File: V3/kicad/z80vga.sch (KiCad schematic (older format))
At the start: 11 parts, among them J1000 Barrel_Jack_Switch, U1000 L7805

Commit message: still trying to make routes work
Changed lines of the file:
@@
 F0 "2000_Z80" 50
 F1 "2000_Z80.sch" 50
-F2 "A[0..19]" T R 5100 3800 50
-F3 "D[0..7]" T R 5100 4600 50
-F4 "WRITE" O R 5100 4000 50
-F5 "READ" O R 5100 3900 50
-F6 "ROM_CS" O R 5100 4300 50
-F7 "RAM_CS" O R 5100 4200 50
+F2 "D[0..7]" T R 5100 4600 50
+F3 "WRITE" O R 5100 4000 50
+F4 "READ" O R 5100 3900 50
+F5 "ROM_CS" O R 5100 4300 50
+F6 "RAM_CS" O R 5100 4200 50
+F7 "A[0..19]" O R 5100 3800 50
 $EndSheet
 Text Notes 7800 6950 0    118  ~ 24

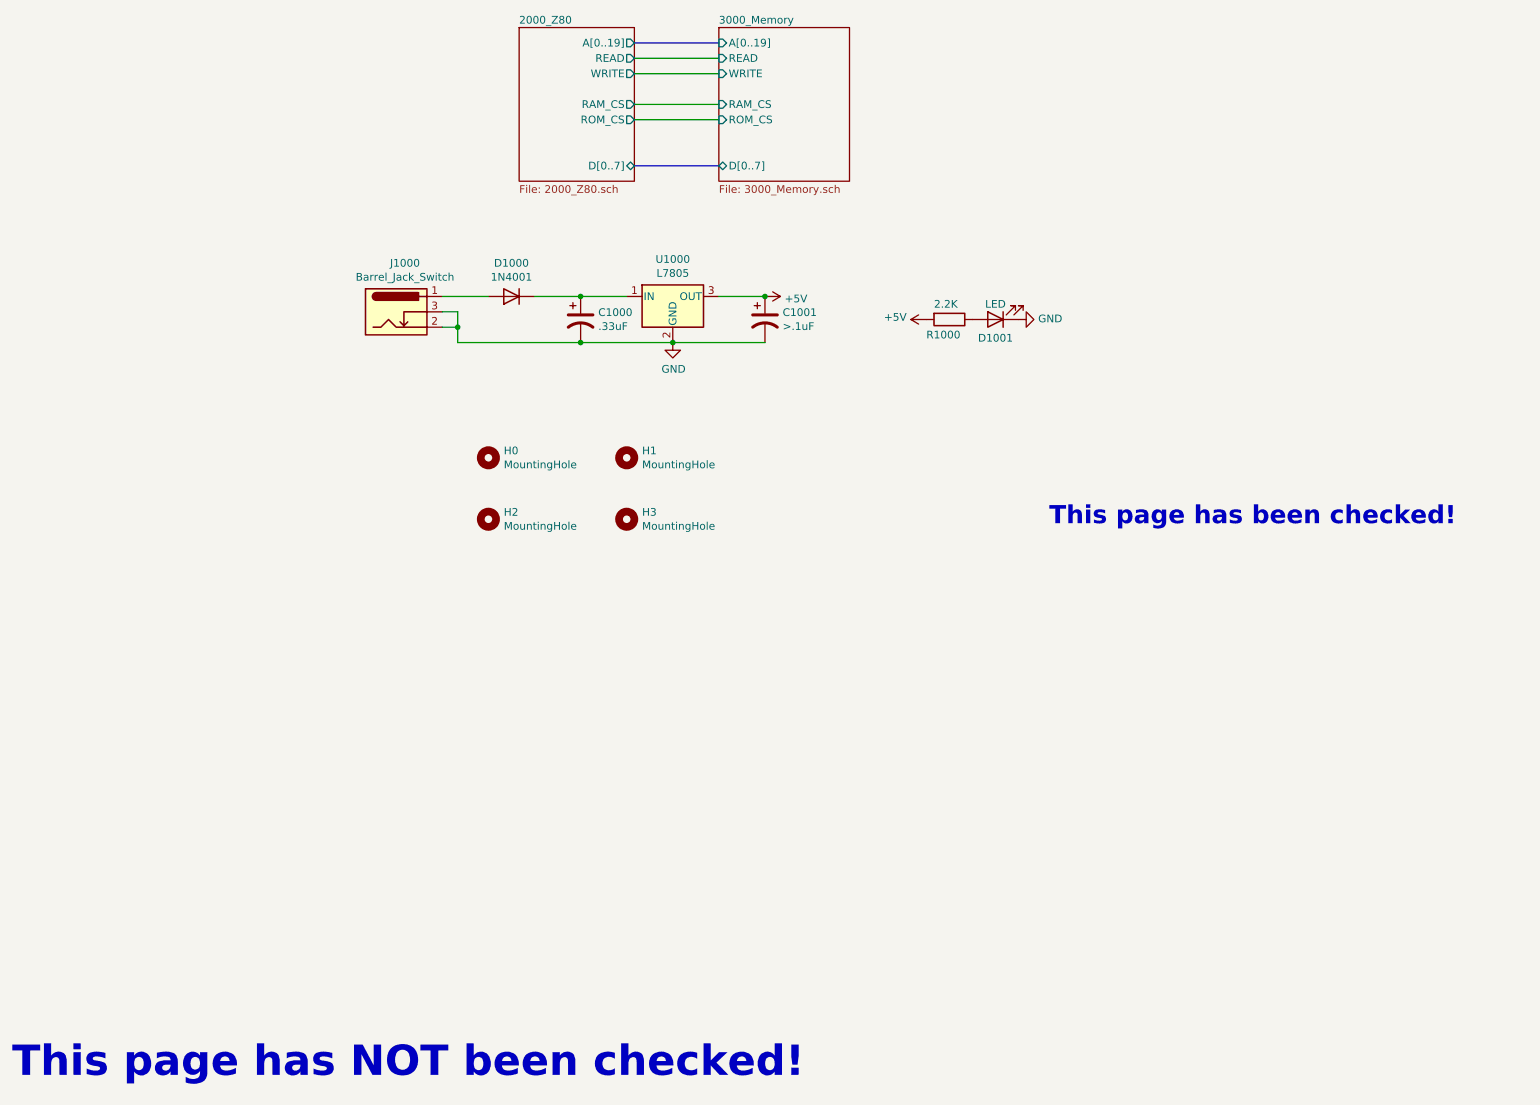
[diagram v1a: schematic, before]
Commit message: Completely redesigned board layout
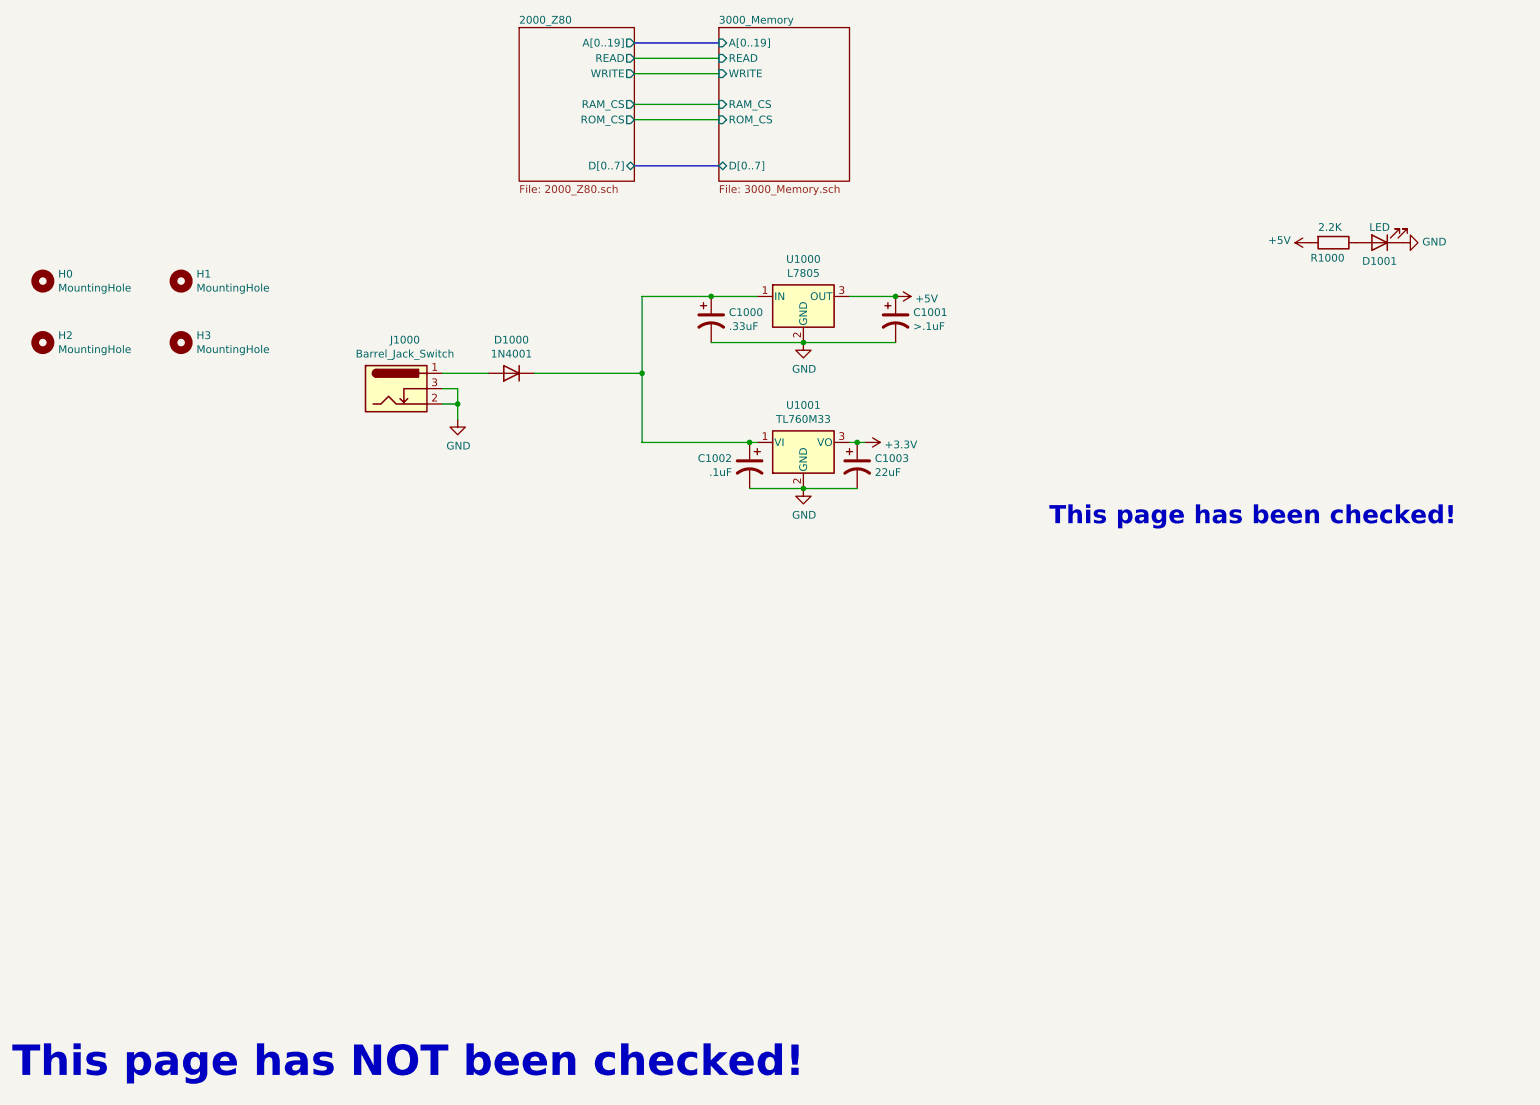
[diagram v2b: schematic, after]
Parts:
- added C1002: .1uF, Capacitor_THT:CP_Radial_D5.0mm_P2.00mm, symbol Device:CP1
- added C1003: 22uF, Capacitor_THT:CP_Radial_D5.0mm_P2.00mm, symbol Device:CP1
- added U1001: TL760M33, Package_TO_SOT_SMD:TO-252-3_TabPin2, symbol Regulator_Linear:LD39150DT33
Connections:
- net GND: now also C1002.2, C1003.2, U1001.2 (GND)
- net at C1000.1, D1000.1 (K), U1000.1 (IN): now also C1002.1, U1001.1 (VI)
- new net +3V3: C1003.1, U1001.3 (VO)
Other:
- moved on the sheet: C1000, C1001, D1000, D1001, H0, H1, H2, H3, J1000, R1000, U1000

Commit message: Final checks and DRC
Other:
- moved on the sheet: D1001, R1000
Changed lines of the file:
@@
 L Device:LED D?
 U 1 1 62A5A6D1
-P 9950 5100
+P 4150 7050
 AR Path="/6191B6A2/61EBDADB/62A5A6D1" Ref="D?"  Part="1"
 AR Path="/62A5A6D1" Ref="D1001"  Part="1"
-F 0 "D1001" H 9950 5250 50  0000 C TNN
-F 1 "LED" H 9950 5000 50  0000 C CNN
-F 2 "LED_THT:LED_D3.0mm" H 9950 5100 50  0001 C CNN
-F 3 "~" H 9950 5100 50  0001 C CNN
-	1    9950 5100
+F 0 "D1001" H 4150 7200 50  0000 C TNN
+F 1 "LED" H 4150 6950 50  0000 C CNN
+F 2 "LED_THT:LED_D3.0mm" H 4150 7050 50  0001 C CNN
+F 3 "~" H 4150 7050 50  0001 C CNN
+	1    4150 7050
 	-1   0    0    1
 $EndComp
@@
 L power:GND #PWR?
 U 1 1 62A5A6D8
-P 10100 5100
+P 4300 7050
 AR Path="/6191B6A2/61EBDADB/62A5A6D8" Ref="#PWR?"  Part="1"
 AR Path="/62A5A6D8" Ref="#PWR0123"  Part="1"
-F 0 "#PWR0123" H 10100 4850 50  0001 C CNN
-F 1 "GND" V 10105 4972 50  0000 R CNN
-F 2 "" H 10100 5100 50  0001 C CNN
-F 3 "" H 10100 5100 50  0001 C CNN
-	1    10100 5100
+F 0 "#PWR0123" H 4300 6800 50  0001 C CNN
+F 1 "GND" V 4305 6922 50  0000 R CNN
+F 2 "" H 4300 7050 50  0001 C CNN
+F 3 "" H 4300 7050 50  0001 C CNN
+	1    4300 7050
 	0    -1   -1   0
 $EndComp
@@
 L power:+5V #PWR0144
 U 1 1 62A5BC7A
-P 9500 5100
-F 0 "#PWR0144" H 9500 4950 50  0001 C CNN
-F 1 "+5V" V 9515 5228 50  0000 L CNN
-F 2 "" H 9500 5100 50  0001 C CNN
-F 3 "" H 9500 5100 50  0001 C CNN
-	1    9500 5100
+P 3700 7050
+F 0 "#PWR0144" H 3700 6900 50  0001 C CNN
+F 1 "+5V" V 3715 7178 50  0000 L CNN
+F 2 "" H 3700 7050 50  0001 C CNN
+F 3 "" H 3700 7050 50  0001 C CNN
+	1    3700 7050
 	0    -1   -1   0
 $EndComp
@@
 L Device:R R?
 U 1 1 62A654EB
-P 9650 5100
+P 3850 7050
 AR Path="/6191B6A2/61EBDADB/62542978/62A654EB" Ref="R?"  Part="1"
 AR Path="/62A654EB" Ref="R1000"  Part="1"
-F 0 "R1000" V 9750 4950 50  0000 L CNN
-F 1 "2.2K" V 9550 5000 50  0000 L CNN
-F 2 "Resistor_THT:R_Axial_DIN0309_L9.0mm_D3.2mm_P2.54mm_Vertical" V 9580 5100 50  0001 C CNN
-F 3 "~" H 9650 5100 50  0001 C CNN
-	1    9650 5100
+F 0 "R1000" V 3950 6900 50  0000 L CNN
+F 1 "2.2K" V 3750 6950 50  0000 L CNN
+F 2 "Resistor_THT:R_Axial_DIN0309_L9.0mm_D3.2mm_P2.54mm_Vertical" V 3780 7050 50  0001 C CNN
+F 3 "~" H 3850 7050 50  0001 C CNN
+	1    3850 7050
 	0    1    1    0
 $EndComp

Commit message: just totally redid the whole thing
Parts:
- removed C1000: .33uF, Capacitor_THT:CP_Radial_D5.0mm_P2.00mm, symbol Device:CP1
- removed C1001: >.1uF, Capacitor_THT:CP_Radial_D5.0mm_P2.00mm, symbol Device:CP1
- removed C1002: .1uF, Capacitor_THT:CP_Radial_D5.0mm_P2.00mm, symbol Device:CP1
- removed C1003: 22uF, Capacitor_THT:CP_Radial_D5.0mm_P2.00mm, symbol Device:CP1
- removed D1000: 1N4001, Diode_THT:D_DO-41_SOD81_P10.16mm_Horizontal, symbol Diode:1N4001
- removed J1000: Barrel_Jack_Switch, Connector_BarrelJack:BarrelJack_Horizontal, symbol Connector:Barrel_Jack_Switch
- removed U1000: L7805, Package_TO_SOT_SMD:TO-263-3_TabPin2, symbol Regulator_Linear:L7805
- removed U1001: TL760M33, Package_TO_SOT_SMD:TO-252-3_TabPin2, symbol Regulator_Linear:LD39150DT33
- R1000: footprint Resistor_THT:R_Axial_DIN0309_L9.0mm_D3.2mm_P2.54mm_Vertical -> Resistor_SMD:R_1206_3216Metric
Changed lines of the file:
@@
 $Descr A4 11693 8268
 encoding utf-8
-Sheet 1 9
+Sheet 1 8
 Title ""
 Date ""
@@
 Wire Wire Line
 	5100 4300 5650 4300
-$Comp
-L Regulator_Linear:L7805 U1000
-U 1 1 6255C02F
-P 6200 5450
-F 0 "U1000" H 6200 5692 50  0000 C CNN
-F 1 "L7805" H 6200 5601 50  0000 C CNN
-F 2 "Package_TO_SOT_SMD:TO-263-3_TabPin2" H 6225 5300 50  0001 L CIN
-F 3 "http://www.st.com/content/ccc/resource/technical/document/datasheet/41/4f/b3/b0/12/d4/47/88/CD00000444.pdf/files/CD00000444.pdf/jcr:content/translations/en.CD00000444.pdf" H 6200 5400 50  0001 C CNN
-	1    6200 5450
-	1    0    0    -1
-$EndComp
-$Comp
-L Device:CP1 C1000
-U 1 1 6255CCA4
-P 5600 5600
-F 0 "C1000" H 5715 5646 50  0000 L CNN
-F 1 ".33uF" H 5715 5555 50  0000 L CNN
-F 2 "Capacitor_THT:CP_Radial_D5.0mm_P2.00mm" H 5600 5600 50  0001 C CNN
-F 3 "~" H 5600 5600 50  0001 C CNN
-	1    5600 5600
-	1    0    0    -1
-$EndComp
-$Comp
-L Device:CP1 C1001
-U 1 1 6255DB35
-P 6800 5600
-F 0 "C1001" H 6915 5646 50  0000 L CNN
-F 1 ">.1uF" H 6915 5555 50  0000 L CNN
-F 2 "Capacitor_THT:CP_Radial_D5.0mm_P2.00mm" H 6800 5600 50  0001 C CNN
-F 3 "~" H 6800 5600 50  0001 C CNN
-	1    6800 5600
-	1    0    0    -1
-$EndComp
-Wire Wire Line
-	5600 5450 5900 5450
-Wire Wire Line
-	6500 5450 6800 5450
-Wire Wire Line
-	5600 5750 6200 5750
-Connection ~ 6200 5750
-Wire Wire Line
-	6200 5750 6800 5750
-$Comp
-L power:GND #PWR0119
-U 1 1 6255E2E4
-P 6200 5750
-F 0 "#PWR0119" H 6200 5500 50  0001 C CNN
-F 1 "GND" H 6205 5577 50  0000 C CNN
-F 2 "" H 6200 5750 50  0001 C CNN
-F 3 "" H 6200 5750 50  0001 C CNN
-	1    6200 5750
-	1    0    0    -1
-$EndComp
-$Comp
-L power:+5V #PWR0141
-U 1 1 6255EB09
-P 6800 5450
-F 0 "#PWR0141" H 6800 5300 50  0001 C CNN
-F 1 "+5V" V 6815 5578 50  0000 L CNN
-F 2 "" H 6800 5450 50  0001 C CNN
-F 3 "" H 6800 5450 50  0001 C CNN
-	1    6800 5450
-	0    1    1    0
-$EndComp
-Connection ~ 6800 5450
-$Comp
-L Connector:Barrel_Jack_Switch J1000
-U 1 1 62560114
-P 3550 6050
-F 0 "J1000" H 3607 6367 50  0000 C CNN
-F 1 "Barrel_Jack_Switch" H 3607 6276 50  0000 C CNN
-F 2 "Connector_BarrelJack:BarrelJack_Horizontal" H 3600 6010 50  0001 C CNN
-F 3 "~" H 3600 6010 50  0001 C CNN
-	1    3550 6050
-	1    0    0    -1
-$EndComp
-Wire Wire Line
-	3850 5950 4150 5950
-Wire Wire Line
-	3850 6050 3950 6050
-Wire Wire Line
-	3950 6050 3950 6150
-Wire Wire Line
-	3950 6150 3850 6150
-Wire Wire Line
-	3950 6150 3950 6250
-Connection ~ 3950 6150
-$Comp
-L Diode:1N4001 D1000
-U 1 1 62563A78
-P 4300 5950
-F 0 "D1000" H 4300 5733 50  0000 C CNN
-F 1 "1N4001" H 4300 5824 50  0000 C CNN
-F 2 "Diode_THT:D_DO-41_SOD81_P10.16mm_Horizontal" H 4300 5775 50  0001 C CNN
-F 3 "http://www.vishay.com/docs/88503/1n4001.pdf" H 4300 5950 50  0001 C CNN
-	1    4300 5950
-	-1   0    0    1
-$EndComp
 $Comp
 L Mechanical:MountingHole H0
@@
 F 0 "R1000" V 3950 6900 50  0000 L CNN
 F 1 "2.2K" V 3750 6950 50  0000 L CNN
-F 2 "Resistor_THT:R_Axial_DIN0309_L9.0mm_D3.2mm_P2.54mm_Vertical" V 3780 7050 50  0001 C CNN
+F 2 "Resistor_SMD:R_1206_3216Metric" V 3780 7050 50  0001 C CNN
 F 3 "~" H 3850 7050 50  0001 C CNN
 	1    3850 7050
 	0    1    1    0
 $EndComp
-$Comp
-L Regulator_Linear:LD39150DT33 U?
-U 1 1 6290B173
-P 6200 6400
-AR Path="/6191B6A2/61F28B7D/6290B173" Ref="U?"  Part="1"
-AR Path="/6191B6A2/61F28B7D/62590ED9/6290B173" Ref="U?"  Part="1"
-AR Path="/6290B173" Ref="U1001"  Part="1"
-F 0 "U1001" H 6200 6642 50  0000 C CNN
-F 1 "TL760M33" H 6200 6551 50  0000 C CNN
-F 2 "Package_TO_SOT_SMD:TO-252-3_TabPin2" H 6200 6600 50  0001 C CNN
-F 3 "https://www.st.com/resource/en/datasheet/ld39150.pdf" H 6300 6150 50  0001 C CNN
-	1    6200 6400
-	1    0    0    -1
-$EndComp
-$Comp
-L power:+3.3V #PWR?
-U 1 1 6290B179
-P 6600 6400
-AR Path="/6191B6A2/61F28B7D/6290B179" Ref="#PWR?"  Part="1"
-AR Path="/6191B6A2/61F28B7D/62590ED9/6290B179" Ref="#PWR?"  Part="1"
-AR Path="/6290B179" Ref="#PWR0120"  Part="1"
-F 0 "#PWR0120" H 6600 6250 50  0001 C CNN
-F 1 "+3.3V" V 6615 6528 50  0000 L CNN
-F 2 "" H 6600 6400 50  0001 C CNN
-F 3 "" H 6600 6400 50  0001 C CNN
-	1    6600 6400
-	0    1    1    0
-$EndComp
-$Comp
-L power:GND #PWR?
-U 1 1 6290B17F
-P 6200 6700
-AR Path="/6191B6A2/61F28B7D/6290B17F" Ref="#PWR?"  Part="1"
-AR Path="/6191B6A2/61F28B7D/62590ED9/6290B17F" Ref="#PWR?"  Part="1"
-AR Path="/6290B17F" Ref="#PWR0124"  Part="1"
-F 0 "#PWR0124" H 6200 6450 50  0001 C CNN
-F 1 "GND" H 6205 6527 50  0000 C CNN
-F 2 "" H 6200 6700 50  0001 C CNN
-F 3 "" H 6200 6700 50  0001 C CNN
-	1    6200 6700
-	1    0    0    -1
-$EndComp
-Wire Wire Line
-	5850 6700 6200 6700
-Wire Wire Line
-	6200 6700 6550 6700
-Connection ~ 6200 6700
-$Comp
-L Device:CP1 C1003
-U 1 1 6290B18E
-P 6550 6550
-AR Path="/6290B18E" Ref="C1003"  Part="1"
-AR Path="/6191B6A2/61F28B7D/62590ED9/6290B18E" Ref="C?"  Part="1"
-F 0 "C1003" H 6665 6596 50  0000 L CNN
-F 1 "22uF" H 6665 6505 50  0000 L CNN
-F 2 "Capacitor_THT:CP_Radial_D5.0mm_P2.00mm" H 6550 6550 50  0001 C CNN
-F 3 "~" H 6550 6550 50  0001 C CNN
-	1    6550 6550
-	1    0    0    -1
-$EndComp
-Wire Wire Line
-	6500 6400 6550 6400
-Connection ~ 6550 6400
-Wire Wire Line
-	6550 6400 6600 6400
-Wire Wire Line
-	5850 6400 5900 6400
-$Comp
-L Device:CP1 C1002
-U 1 1 6290B196
-P 5850 6550
-AR Path="/6290B196" Ref="C1002"  Part="1"
-AR Path="/6191B6A2/61F28B7D/62590ED9/6290B196" Ref="C?"  Part="1"
-F 0 "C1002" H 5965 6596 50  0000 L CNN
-F 1 ".1uF" H 5965 6505 50  0000 L CNN
-F 2 "Capacitor_THT:CP_Radial_D5.0mm_P2.00mm" H 5850 6550 50  0001 C CNN
-F 3 "~" H 5850 6550 50  0001 C CNN
-	1    5850 6550
-	-1   0    0    -1
-$EndComp
-$Comp
-L power:GND #PWR0140
-U 1 1 629120EB
-P 3950 6250
-F 0 "#PWR0140" H 3950 6000 50  0001 C CNN
-F 1 "GND" H 3955 6077 50  0000 C CNN
-F 2 "" H 3950 6250 50  0001 C CNN
-F 3 "" H 3950 6250 50  0001 C CNN
-	1    3950 6250
-	1    0    0    -1
-$EndComp
-Wire Wire Line
-	4450 5950 5150 5950
-Wire Wire Line
-	5150 5950 5150 5450
-Wire Wire Line
-	5150 5450 5600 5450
-Connection ~ 5600 5450
-Wire Wire Line
-	5150 5950 5150 6400
-Wire Wire Line
-	5150 6400 5850 6400
-Connection ~ 5150 5950
-Connection ~ 5850 6400
 $EndSCHEMATC

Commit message: More rearranging
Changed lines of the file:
@@
 Wire Bus Line
 	5100 3800 5650 3800
-Wire Wire Line
-	5100 3900 5650 3900
-Wire Wire Line
-	5100 4000 5650 4000
 $Sheet
 S 5650 3700 850  1000
@@
 F3 "D[0..7]" B L 5650 4600 50
 F4 "ROM_CS" I L 5650 4300 50
-F5 "READ" I L 5650 3900 50
-F6 "RAM_CS" I L 5650 4200 50
-F7 "WRITE" I L 5650 4000 50
+F5 "RAM_CS" I L 5650 4200 50
+F6 "RD" I L 5650 3900 50
+F7 "WR" I L 5650 4000 50
 $EndSheet
 $Sheet
@@
 F1 "2000_Z80.sch" 50
 F2 "D[0..7]" T R 5100 4600 50
-F3 "WRITE" O R 5100 4000 50
-F4 "READ" O R 5100 3900 50
-F5 "ROM_CS" O R 5100 4300 50
-F6 "RAM_CS" O R 5100 4200 50
-F7 "A[0..19]" O R 5100 3800 50
+F3 "ROM_CS" O R 5100 4300 50
+F4 "RAM_CS" O R 5100 4200 50
+F5 "A[0..19]" O R 5100 3800 50
+F6 "WR" O R 5100 4000 50
+F7 "RD" O R 5100 3900 50
 $EndSheet
 Text Notes 7800 6950 0    118  ~ 24
@@
 	0    1    1    0
 $EndComp
+Wire Wire Line
+	5100 3900 5650 3900
+Wire Wire Line
+	5100 4000 5650 4000
 $EndSCHEMATC

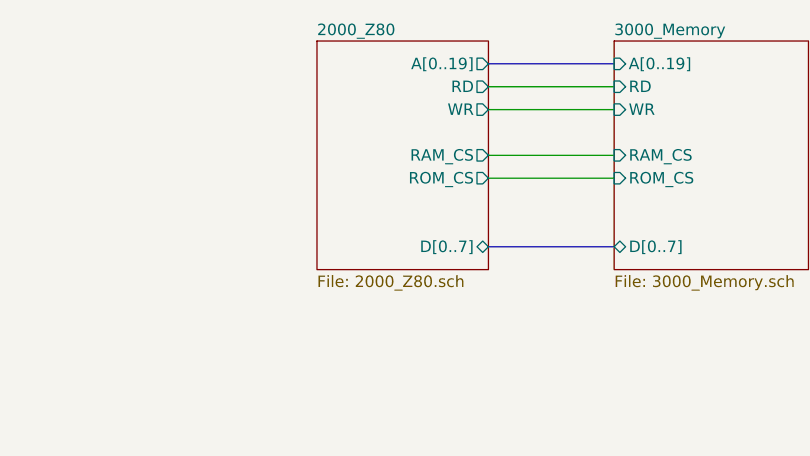
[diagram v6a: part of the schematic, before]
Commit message: 3.1 fix sheet hierarchy (#13)
* Fixed Schematic Heirarchy issue

* some footprints re-added to board

* Add footprints added

* Minor changes
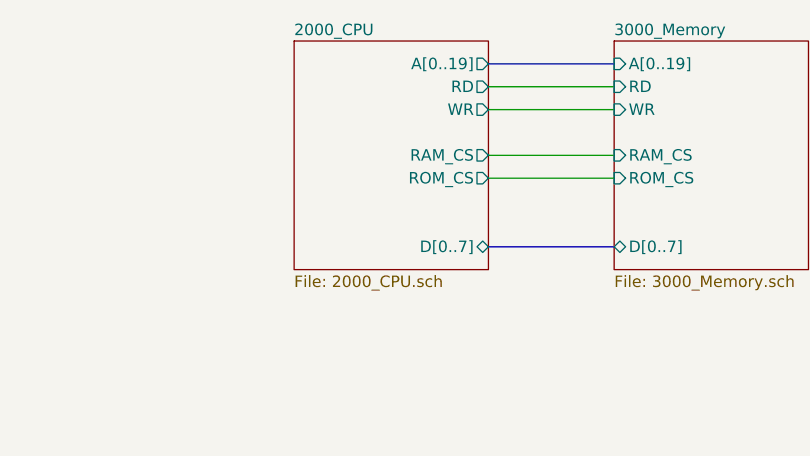
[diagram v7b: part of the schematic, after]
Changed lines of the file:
@@
 $Descr A4 11693 8268
 encoding utf-8
-Sheet 1 7
+Sheet 1 6
 Title ""
 Date ""
@@
 F6 "RD" I L 5650 3900 50
 F7 "WR" I L 5650 4000 50
-$EndSheet
-$Sheet
-S 4350 3700 750  1000
-U 6191B6A2
-F0 "2000_Z80" 50
-F1 "2000_Z80.sch" 50
-F2 "D[0..7]" T R 5100 4600 50
-F3 "ROM_CS" O R 5100 4300 50
-F4 "RAM_CS" O R 5100 4200 50
-F5 "A[0..19]" O R 5100 3800 50
-F6 "WR" O R 5100 4000 50
-F7 "RD" O R 5100 3900 50
 $EndSheet
 Text Notes 7800 6950 0    118  ~ 24
@@
 Wire Wire Line
 	5100 4000 5650 4000
+$Sheet
+S 4250 3700 850  1000
+U 63A83936
+F0 "2000_CPU" 50
+F1 "2000_CPU.sch" 50
+F2 "A[0..19]" O R 5100 3800 50
+F3 "RD" O R 5100 3900 50
+F4 "ROM_CS" O R 5100 4300 50
+F5 "RAM_CS" O R 5100 4200 50
+F6 "D[0..7]" B R 5100 4600 50
+F7 "WR" O R 5100 4000 50
+$EndSheet
 $EndSCHEMATC
